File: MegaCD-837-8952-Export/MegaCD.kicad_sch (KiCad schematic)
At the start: 154 parts, among them CN1 CON 25P ANGLE, CN2 EDGE 60P, CN3 CON 21P, IC1 68HC000, IC10 TC51832, IC11 TC51832, IC12 74HC86, IC13 LC8951, IC14 MB8464A-90L, IC15 MB8464A-90L, IC16 MB8464A-10L, IC17 74AC74, IC2 315-5548/315-5632, IC3 315-5476A, IC4 27C1024, IC5 HM514270, IC6 MB3790, IC7 TC511664BZ, IC8 TC511664BZ, IC9 74HC245, J2 2TS, J3 MH, J4 CAS0, M0 TestPoint, M1 TestPoint, M10 TestPoint, M11 TestPoint, M12 TestPoint, M13 TestPoint, M14 TestPoint, M192 TestPoint, M2 TestPoint, M3 TestPoint, M4 TestPoint, M5 TestPoint, M57 TestPoint, M6 TestPoint, M7 TestPoint, M8 TestPoint, M9 TestPoint

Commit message: First pass routing, add inner layers.
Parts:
- removed CW51: 22nF, MegaCD_Footprints:SMD_0805_HandSolder, symbol Device:C
- removed CX47: 200pF, MegaCD_Footprints:SMD_0805_HandSolder, symbol Device:C_Polarized
- added C12, C19: 22nF, MegaCD_Footprints:SMD_0805_HandSolder, symbol Device:C
- added C13, C20, C22, C29, C34, C35, C36, C39, C5, C54, C55, C56, C8: ?F, MegaCD_Footprints:SMD_0805_HandSolder, symbol Device:C
- added C21, C32, C37, C53, C57, C58: 0, MegaCD_Footprints:SMD_0805_HandSolder, symbol Device:C
- added C44: 10uF, MegaCD_Footprints:CP_Elec_3x5.4, symbol Device:C_Polarized
- added FB10, FB11, FB9: ~, MegaCD_Footprints:SMD_0805_HandSolder_Narrow, symbol Device:FerriteBead_Small
- added FB18, FB4: ~, MegaCD_Footprints:FB_SMD_Large, symbol Device:FerriteBead_Small
- added ICY17: 74AC74, MegaCD_Footprints:SOIC-14W_5.3mm_P1.27mm, symbol 74xx:74HC74
- added R8, R9: 0, MegaCD_Footprints:SMD_0805_HandSolder, symbol Device:R
- C38: value 22nF -> 0
- CY16: renamed from C16; now left out of the parts list
- CY52: renamed from CX52; now left out of the parts list
- CY54: renamed from C54; now left out of the parts list
- CY56: renamed from C56; now left out of the parts list
- CY57: renamed from C57; now left out of the parts list
- CY58: renamed from C58; now left out of the parts list
- FB1: renamed from FB5; footprint MegaCD_Footprints:SMD_0805_HandSolder_Narrow -> MegaCD_Footprints:FB_P7.00mm
- FB5: renamed from FB1; footprint MegaCD_Footprints:FB_P7.00mm -> MegaCD_Footprints:SMD_0805_HandSolder_Narrow
- J1, J2, J3, J4, J5, M192, M57: now left out of the parts list
- renumbered CX30 to C10, C36 to C16, C29 to C23, C35 to C24, CX36 to C25, C32 to C26, C33 to C27, C34 to C28, C55 to C33, C27 to C9, C20 to CY20, CX53 to CY53, R7 to R3, R6 to R4, RG5 to R6, R4 to R7, TR2 to TR1, TR1 to TR2
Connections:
- net 12M: now also C34.1
- net 50M: now also ICY17.3 (C)
- net BCLK: now also FB7.1, FB7.2
- net CDCKD: now also FB9.1, FB9.2
- net D10: now also C21.1
- net DFCK: now also FB5.1, FB5.2
- net DFCKBF: now also C55.1
- net GND: now also CN2.a2 (Pin_a2), EM1.2, EM2.2, EM3.2, C12.2, C13.2, C19.1, C20.2, C21.2, C29.2, C32.2, C35.2, C36.2, C37.2, C39.2, C44.2, C5.2, C53.2, C55.2, C56.2, C57.2, C58.2, C8.2, ICY17.7 (GND)
- net LRCK: now also FB6.1, FB6.2
- net LRCKB: now also FB13.1; no longer CN3.5 (Pin_5), IC13.32 (LRCK), IC2.75 (LRCK)
- net PBCLKF: now also C54.2
- net PDATA: now also C35.1
- net PLRCK: now also C57.1, R8.1, R8.2, R9.1, R9.2
- net PWCLK: now also C58.1
- net RAS2: now also ICY17.6 (~{Q})
- net SBSOB: now also FB11.1, FB11.2
- net SCOR: now also FB8.1, FB8.2
- net VCC2: now also EM1.1, EM1.3, EM2.1, EM2.3, EM3.1, EM3.3, C12.1, C13.1, C19.2, C20.1, C22.2, C34.2, C44.1, C5.1, C54.1, C8.1, FB18.1, FB18.2, FB4.1, FB4.2, ICY17.1 (~{R}), ICY17.10 (~{S}), ICY17.11 (C), ICY17.12 (D), ICY17.13 (~{R}), ICY17.14 (VCC), ICY17.4 (~{S}); no longer C38.1
- net WD3: now also C38.1
- net WD5: now also FB16.1; no longer IC3.46 (RAMAD5)
- net WFCKD: now also FB10.1, FB10.2
- net ~{CLWEX}: now also R11.1, C53.1
- net ~{CLWEY}: no longer R11.1
- net ~{PCAS}: now also C22.1
- net ~{PRAS}: now also C32.1
- net ~{RAS2X}: now also ICY17.2 (D)
- net ~{RAS2}: now also ICY17.5 (Q)
- net ~{ROE}: now also C37.1
- net WD5F: now reaches FB16.2
- net WD5F: now also IC3.46 (RAMAD5), C29.1
- net LRCKBF: now reaches FB13.2
- net LRCKBF: now also CN3.5 (Pin_5), IC13.32 (LRCK), IC2.75 (LRCK), C36.1, C56.1
- no-connect marks 56 -> 57
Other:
- note added: "MCE2/MCE3 EXPORT BOARD"
- note removed: "Alternative for ICs 5-8 on export boards"
- moved on the sheet: C30, C31, C40, EM1, EM2, EM3, FB12, FB13, FB14, FB15, FB16, FB5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

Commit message: Finish off zones/fills.
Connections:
- net GND: now also C22.2, C34.2, C54.1; no longer CN2.a2 (Pin_a2)
- net VCC2: no longer C22.2, C34.2, C54.1
- no-connect marks 57 -> 58
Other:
- moved on the sheet: C54, FB15
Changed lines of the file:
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@@
   (junction (at 46.99 467.36) (diameter 0) (color 0 0 0 0)
   )
-  (junction (at 745.49 298.45) (diameter 0) (color 0 0 0 0)
-  )
   (junction (at 704.85 233.68) (diameter 0) (color 0 0 0 0)
   )
@@
   (junction (at 519.43 293.37) (diameter 0) (color 0 0 0 0)
   )
-  (junction (at 495.3 506.73) (diameter 0) (color 0 0 0 0)
+  (junction (at 488.95 490.22) (diameter 0) (color 0 0 0 0)
   )
   (junction (at 495.3 515.62) (diameter 0) (color 0 0 0 0)
@@
   (junction (at 45.72 535.94) (diameter 0) (color 0 0 0 0)
   )
+  (junction (at 382.27 510.54) (diameter 0) (color 0 0 0 0)
+  )
   (junction (at 367.03 135.89) (diameter 0) (color 0 0 0 0)
   )
@@
   (junction (at 726.44 168.91) (diameter 0) (color 0 0 0 0)
   )
-  (junction (at 382.27 502.92) (diameter 0) (color 0 0 0 0)
-  )
   (junction (at 330.2 336.55) (diameter 0) (color 0 0 0 0)
   )
@@
   (junction (at 812.8 95.25) (diameter 0) (color 0 0 0 0)
   )
+  (junction (at 382.27 518.16) (diameter 0) (color 0 0 0 0)
+  )
   (junction (at 121.92 539.75) (diameter 0) (color 0 0 0 0)
   )
@@
   (no_connect (at 278.13 148.59))
   (no_connect (at 763.27 367.03))
+  (no_connect (at 750.57 300.99))
   (no_connect (at 501.65 318.77))
   (no_connect (at 692.15 251.46))
@@
     (stroke (width 0) (type default))
   )
-  (wire (pts (xy 750.57 300.99) (xy 745.49 300.99))
-    (stroke (width 0) (type default))
-  )
   (bus (pts (xy 339.09 328.93) (xy 339.09 370.84))
     (stroke (width 0) (type default))
@@
     (stroke (width 0) (type default))
   )
-  (wire (pts (xy 495.3 506.73) (xy 492.76 506.73))
+  (wire (pts (xy 488.95 490.22) (xy 486.41 490.22))
     (stroke (width 0) (type default))
   )
@@
     (stroke (width 0) (type default))
   )
-  (wire (pts (xy 482.6 506.73) (xy 487.68 506.73))
+  (wire (pts (xy 476.25 490.22) (xy 481.33 490.22))
     (stroke (width 0) (type default))
   )
@@
     (stroke (width 0) (type default))
   )
-  (wire (pts (xy 495.3 506.73) (xy 495.3 502.92))
-    (stroke (width 0) (type default))
-  )
   (wire (pts (xy 256.54 113.03) (xy 245.11 113.03))
     (stroke (width 0) (type default))
@@
     (stroke (width 0) (type default))
   )
-  (wire (pts (xy 382.27 510.54) (xy 382.27 502.92))
-    (stroke (width 0) (type default))
-  )
   (bus (pts (xy 176.53 341.63) (xy 176.53 339.09))
     (stroke (width 0) (type default))
@@
     (stroke (width 0) (type default))
   )
-  (wire (pts (xy 497.84 506.73) (xy 495.3 506.73))
+  (wire (pts (xy 491.49 490.22) (xy 488.95 490.22))
     (stroke (width 0) (type default))
   )
@@
     (stroke (width 0) (type default))
   )
-  (wire (pts (xy 722.63 298.45) (xy 745.49 298.45))
+  (wire (pts (xy 722.63 298.45) (xy 750.57 298.45))
     (stroke (width 0) (type default))
   )
@@
     (stroke (width 0) (type default))
   )
+  (wire (pts (xy 382.27 510.54) (xy 382.27 518.16))
+    (stroke (width 0) (type default))
+  )
   (wire (pts (xy 642.62 53.34) (xy 645.16 53.34))
     (stroke (width 0) (type default))
@@
     (stroke (width 0) (type default))
   )
-  (wire (pts (xy 495.3 491.49) (xy 495.3 495.3))
-    (stroke (width 0) (type default))
-  )
   (wire (pts (xy 721.36 106.68) (xy 721.36 113.03))
     (stroke (width 0) (type default))
@@
     (stroke (width 0) (type default))
   )
+  (wire (pts (xy 488.95 492.76) (xy 488.95 490.22))
+    (stroke (width 0) (type default))
+  )
   (wire (pts (xy 782.32 110.49) (xy 782.32 111.76))
     (stroke (width 0) (type default))
@@
     (stroke (width 0) (type default))
   )
-  (wire (pts (xy 382.27 495.3) (xy 382.27 502.92))
+  (wire (pts (xy 382.27 510.54) (xy 382.27 502.92))
     (stroke (width 0) (type default))
   )
@@
     (stroke (width 0) (type default))
   )
+  (wire (pts (xy 488.95 500.38) (xy 488.95 502.92))
+    (stroke (width 0) (type default))
+  )
   (wire (pts (xy 518.16 54.61) (xy 518.16 57.15))
     (stroke (width 0) (type default))
@@
     (stroke (width 0) (type default))
   )
-  (wire (pts (xy 745.49 298.45) (xy 750.57 298.45))
-    (stroke (width 0) (type default))
-  )
   (bus (pts (xy 264.16 40.64) (xy 264.16 43.18))
     (stroke (width 0) (type default))
@@
     (stroke (width 0) (type default))
   )
-  (wire (pts (xy 745.49 300.99) (xy 745.49 298.45))
-    (stroke (width 0) (type default))
-  )
   (wire (pts (xy 740.41 302.26) (xy 740.41 303.53))
     (stroke (width 0) (type default))
@@
     )
   )
-  (global_label "PBCLK" (shape input) (at 482.6 506.73 180) (fields_autoplaced)
+  (global_label "PBCLK" (shape input) (at 476.25 490.22 180) (fields_autoplaced)
     (effects (font (size 1.27 1.27)) (justify right))
-    (property "Intersheetrefs" "${INTERSHEET_REFS}" (at 473.5861 506.73 0)
+    (property "Intersheetrefs" "${INTERSHEET_REFS}" (at 467.2361 490.22 0)
       (effects (font (size 1.27 1.27)) (justify right) hide)
     )
@@
     )
   )
-  (global_label "PBCLKF" (shape input) (at 497.84 506.73 0) (fields_autoplaced)
+  (global_label "PBCLKF" (shape input) (at 491.49 490.22 0) (fields_autoplaced)
     (effects (font (size 1.27 1.27)) (justify left))
-    (property "Intersheetrefs" "${INTERSHEET_REFS}" (at 507.9425 506.73 0)
+    (property "Intersheetrefs" "${INTERSHEET_REFS}" (at 501.5925 490.22 0)
       (effects (font (size 1.27 1.27)) (justify left) hide)
     )
@@
     )
   )
-  (symbol (lib_id "Device:C") (at 495.3 499.11 0) (unit 1)
+  (symbol (lib_id "Device:C") (at 488.95 496.57 180) (unit 1)
     (in_bom yes) (on_board yes) (dnp no)
-    (property "Reference" "C54" (at 490.22 496.57 0)
+    (property "Reference" "C54" (at 494.03 499.11 0)
       (effects (font (size 1.27 1.27)) (justify left))
     )
-    (property "Value" "?F" (at 496.57 501.65 0)
+    (property "Value" "?F" (at 487.68 494.03 0)
       (effects (font (size 1.27 1.27)) (justify left))
     )
-    (property "Footprint" "MegaCD_Footprints:SMD_0805_HandSolder" (at 496.2652 502.92 0)
+    (property "Footprint" "MegaCD_Footprints:SMD_0805_HandSolder" (at 487.9848 492.76 0)
       (effects (font (size 1.27 1.27)) hide)
     )
-    (property "Datasheet" "~" (at 495.3 499.11 0)
+    (property "Datasheet" "~" (at 488.95 496.57 0)
       (effects (font (size 1.27 1.27)) hide)
     )
@@
     )
   )
-  (symbol (lib_id "Device:FerriteBead_Small") (at 490.22 506.73 90) (unit 1)
+  (symbol (lib_id "Device:FerriteBead_Small") (at 483.87 490.22 90) (unit 1)
     (in_bom yes) (on_board yes) (dnp no) (fields_autoplaced)
-    (property "Reference" "FB15" (at 490.1819 504.19 90)
+    (property "Reference" "FB15" (at 483.8319 487.68 90)
       (effects (font (size 1.27 1.27)))
     )
-    (property "Value" "~" (at 490.1819 504.19 90)
+    (property "Value" "~" (at 483.8319 487.68 90)
       (effects (font (size 1.27 1.27)))
     )
-    (property "Footprint" "MegaCD_Footprints:FB_P9.00mm" (at 490.22 508.508 90)
+    (property "Footprint" "MegaCD_Footprints:FB_P9.00mm" (at 483.87 491.998 90)
       (effects (font (size 1.27 1.27)) hide)
     )
-    (property "Datasheet" "~" (at 490.22 506.73 0)
+    (property "Datasheet" "~" (at 483.87 490.22 0)
       (effects (font (size 1.27 1.27)) hide)
     )
@@
     )
   )
-  (symbol (lib_id "power:VCC") (at 382.27 495.3 0) (unit 1)
-    (in_bom yes) (on_board yes) (dnp no) (fields_autoplaced)
-    (property "Reference" "#PWR080" (at 382.27 499.11 0)
-      (effects (font (size 1.27 1.27)) hide)
-    )
-    (property "Value" "VCC2" (at 382.27 491.49 0)
-      (effects (font (size 1.27 1.27)))
-    )
-    (property "Footprint" "" (at 382.27 495.3 0)
-      (effects (font (size 1.27 1.27)) hide)
-    )
-    (property "Datasheet" "" (at 382.27 495.3 0)
-      (effects (font (size 1.27 1.27)) hide)
-    )
-    (pin "1")
-    (instances
-      (project "MegaCD"
-        (path "/0cd008a0-ed23-4303-a3f0-e3f038adfe31"
-          (reference "#PWR080") (unit 1)
-        )
-      )
-    )
-  )
   (symbol (lib_id "Device:C") (at 215.9 69.85 0) (unit 1)
     (in_bom no) (on_board no) (dnp no)
@@
     )
   )
-  (symbol (lib_id "power:VCC") (at 495.3 491.49 0) (unit 1)
-    (in_bom yes) (on_board yes) (dnp no) (fields_autoplaced)
-    (property "Reference" "#PWR082" (at 495.3 495.3 0)
-      (effects (font (size 1.27 1.27)) hide)
-    )
-    (property "Value" "VCC2" (at 495.3 487.68 0)
-      (effects (font (size 1.27 1.27)))
-    )
-    (property "Footprint" "" (at 495.3 491.49 0)
-      (effects (font (size 1.27 1.27)) hide)
-    )
-    (property "Datasheet" "" (at 495.3 491.49 0)
-      (effects (font (size 1.27 1.27)) hide)
-    )
-    (pin "1")
-    (instances
-      (project "MegaCD"
-        (path "/0cd008a0-ed23-4303-a3f0-e3f038adfe31"
-          (reference "#PWR082") (unit 1)
-        )
-      )
-    )
-  )
   (symbol (lib_id "Connector:TestPoint") (at 123.19 59.69 0) (unit 1)
     (in_bom yes) (on_board yes) (dnp no)
@@
         )
       )
+    )
+  )
+  (symbol (lib_id "power:GND") (at 488.95 502.92 0) (unit 1)
+    (in_bom yes) (on_board yes) (dnp no)
+    (property "Reference" "#PWR080" (at 488.95 509.27 0)
+      (effects (font (size 1.27 1.27)) hide)
+    )
+    (property "Value" "GND" (at 488.95 506.73 0)
+      (effects (font (size 1.27 1.27)))
+    )
+    (property "Footprint" "" (at 488.95 502.92 0)
+      (effects (font (size 1.27 1.27)) hide)
+    )
+    (property "Datasheet" "" (at 488.95 502.92 0)
+      (effects (font (size 1.27 1.27)) hide)
+    )
+    (pin "1")
+    (instances
+      (project "MegaCD"
+        (path "/0cd008a0-ed23-4303-a3f0-e3f038adfe31"
+          (reference "#PWR080") (unit 1)
+        )
+      )

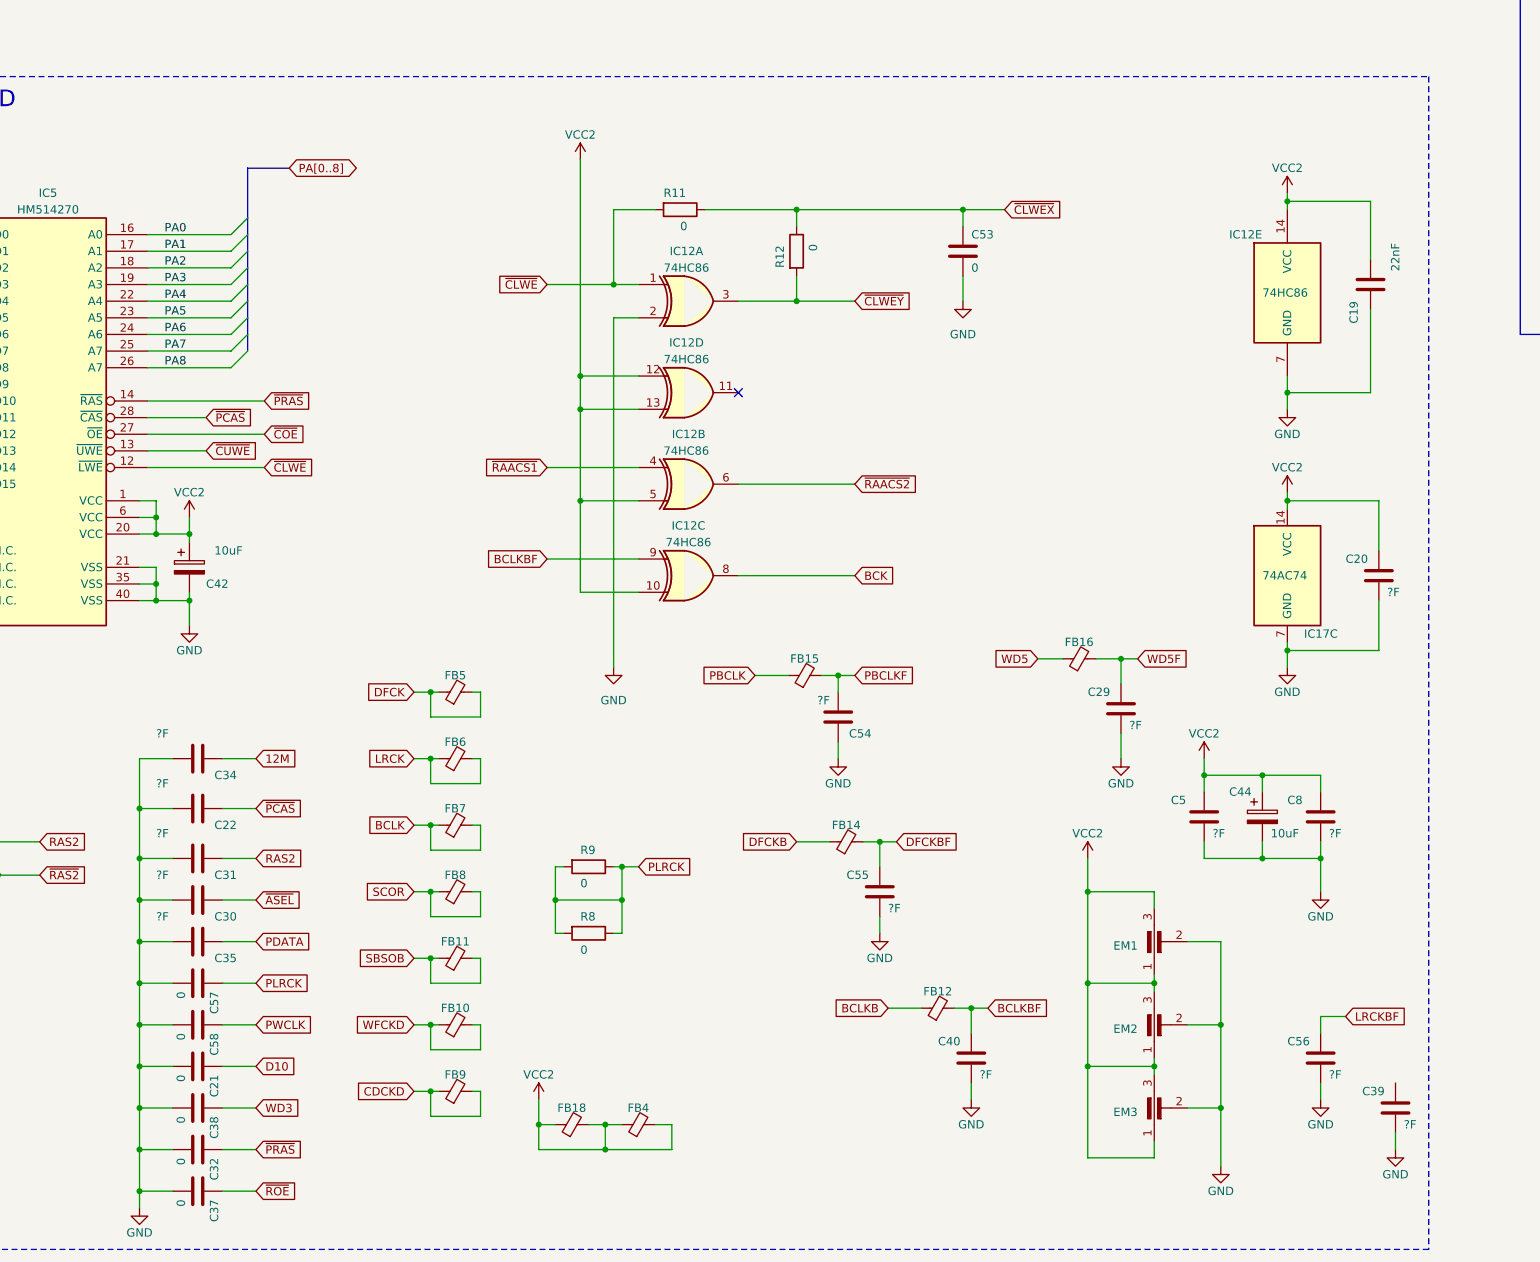
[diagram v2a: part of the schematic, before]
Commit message: Match inner layers to original board, schematic corrections.
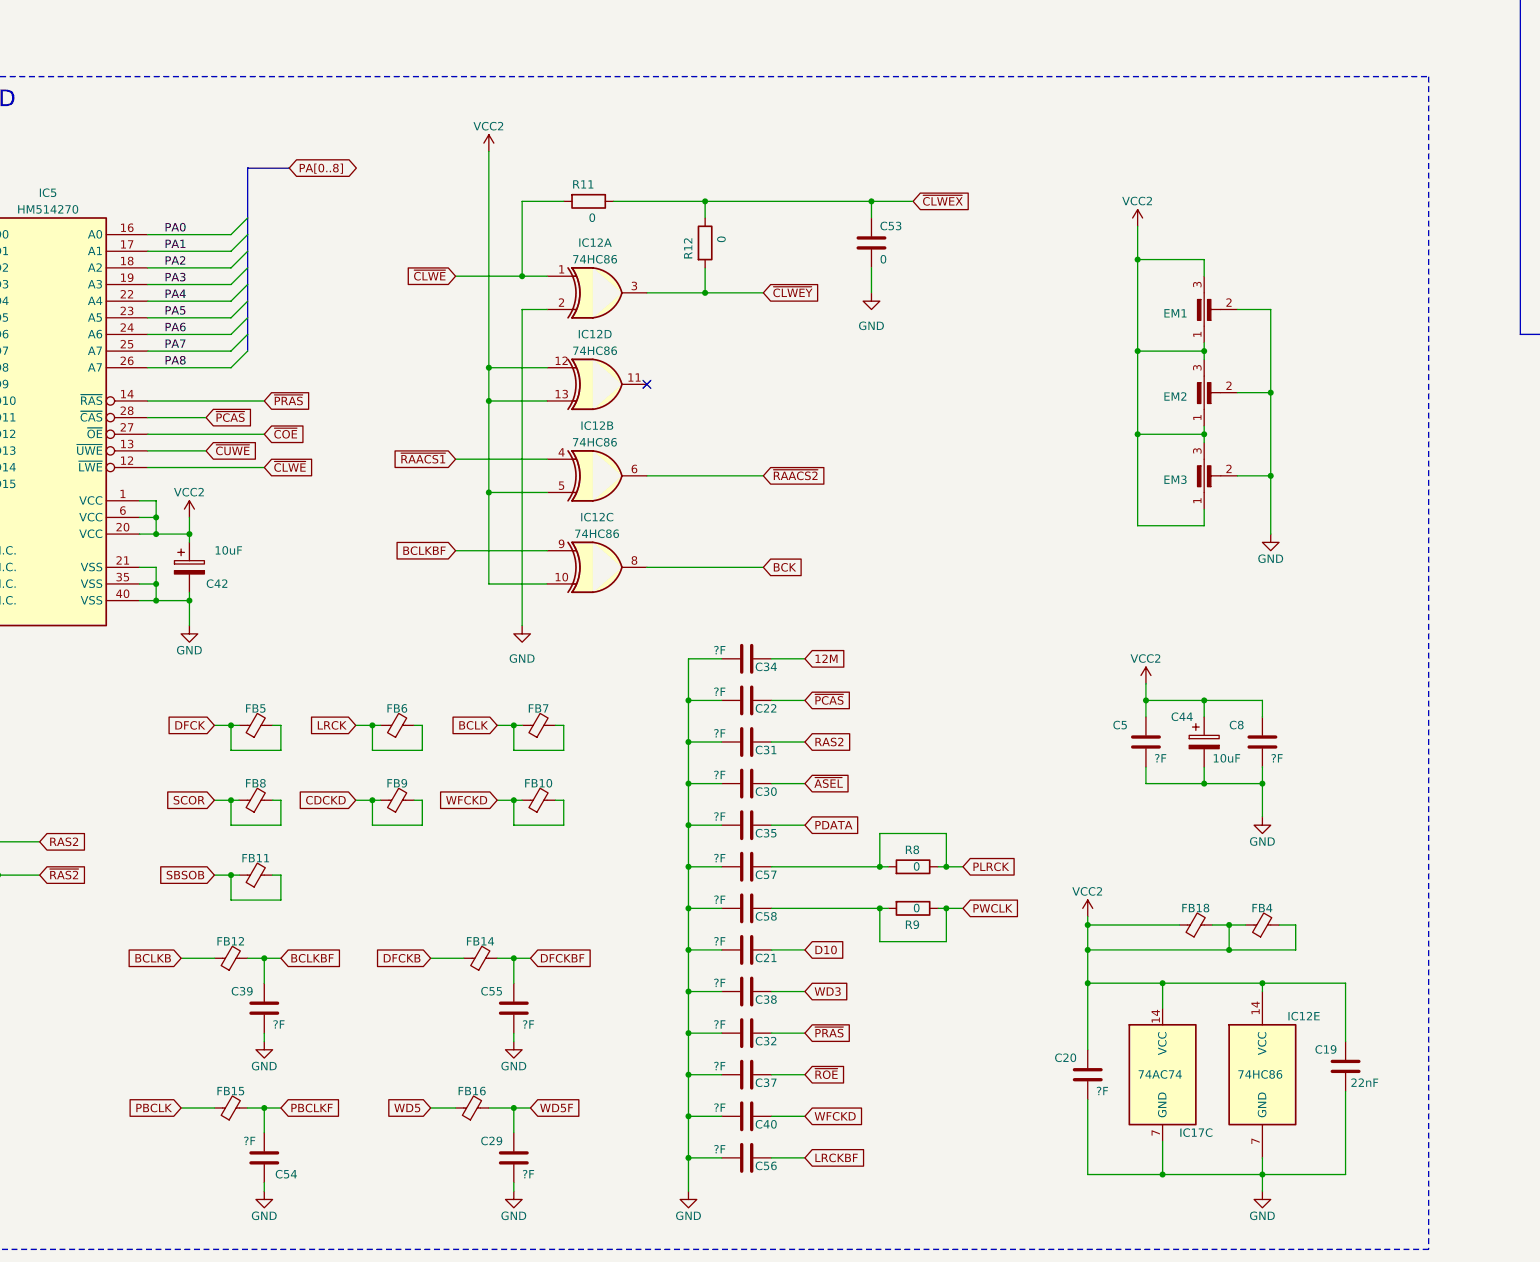
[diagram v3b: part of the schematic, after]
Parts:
- C21, C32, C37, C38, C57, C58: value 0 -> ?F
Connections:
- net BCLKBF: now also C39.1; no longer C40.1
- net PLRCK: no longer R9.1, R9.2
- net PWCLK: now also R9.1, R9.2
- net WFCKD: now also C40.1
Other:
- moved on the sheet: C19, C20, C21, C22, C29, C30, C31, C32, C34, C35, C37, C38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

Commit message: Separate out VCC nets, silkscreen tweaks.
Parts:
- C13: value ?F -> 22uF
- C20, C5, C8: value ?F -> 22nF
- C22, C30, C32, C56, C57, C58: value ?F -> N/U
- C23, C26: value 100pF -> Not used
- C53: value 0 -> Not used
- C54, C55: value ?F -> Not used
- IC10, IC11: value TC51832 -> 65256BLFP-10T
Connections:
- net VCC2: no longer C12.1, C2.1, C41.1, EM1.1, EM2.1, IC1.12 (BGACK), IC1.13 (BR), IC1.14 (VCC), IC1.24 (BERR), IC1.52 (VCC), IC9.20 (VCC), R1.1, R2.1
- new net VCC2B: C12.1, EM2.1, IC9.20 (VCC)
- new net VCC2C: C2.1, C41.1, EM1.1, IC1.12 (BGACK), IC1.13 (BR), IC1.14 (VCC), IC1.24 (BERR), IC1.52 (VCC), R1.1, R2.1
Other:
- note added: "Unpopulated (shorted on board)"
- note removed: "Rev 0: Not used"
- moved on the sheet: C19, C21, C22, C23, C24, C26, C27, C30, C31, C34, C35, C37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
